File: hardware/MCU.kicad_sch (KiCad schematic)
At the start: 15 parts, among them SW1 MCP_HW_ADDR_SEL, SW2 MCP_N_RST, SW3 SW_SYS-PWR, U1 MCP23017_SO

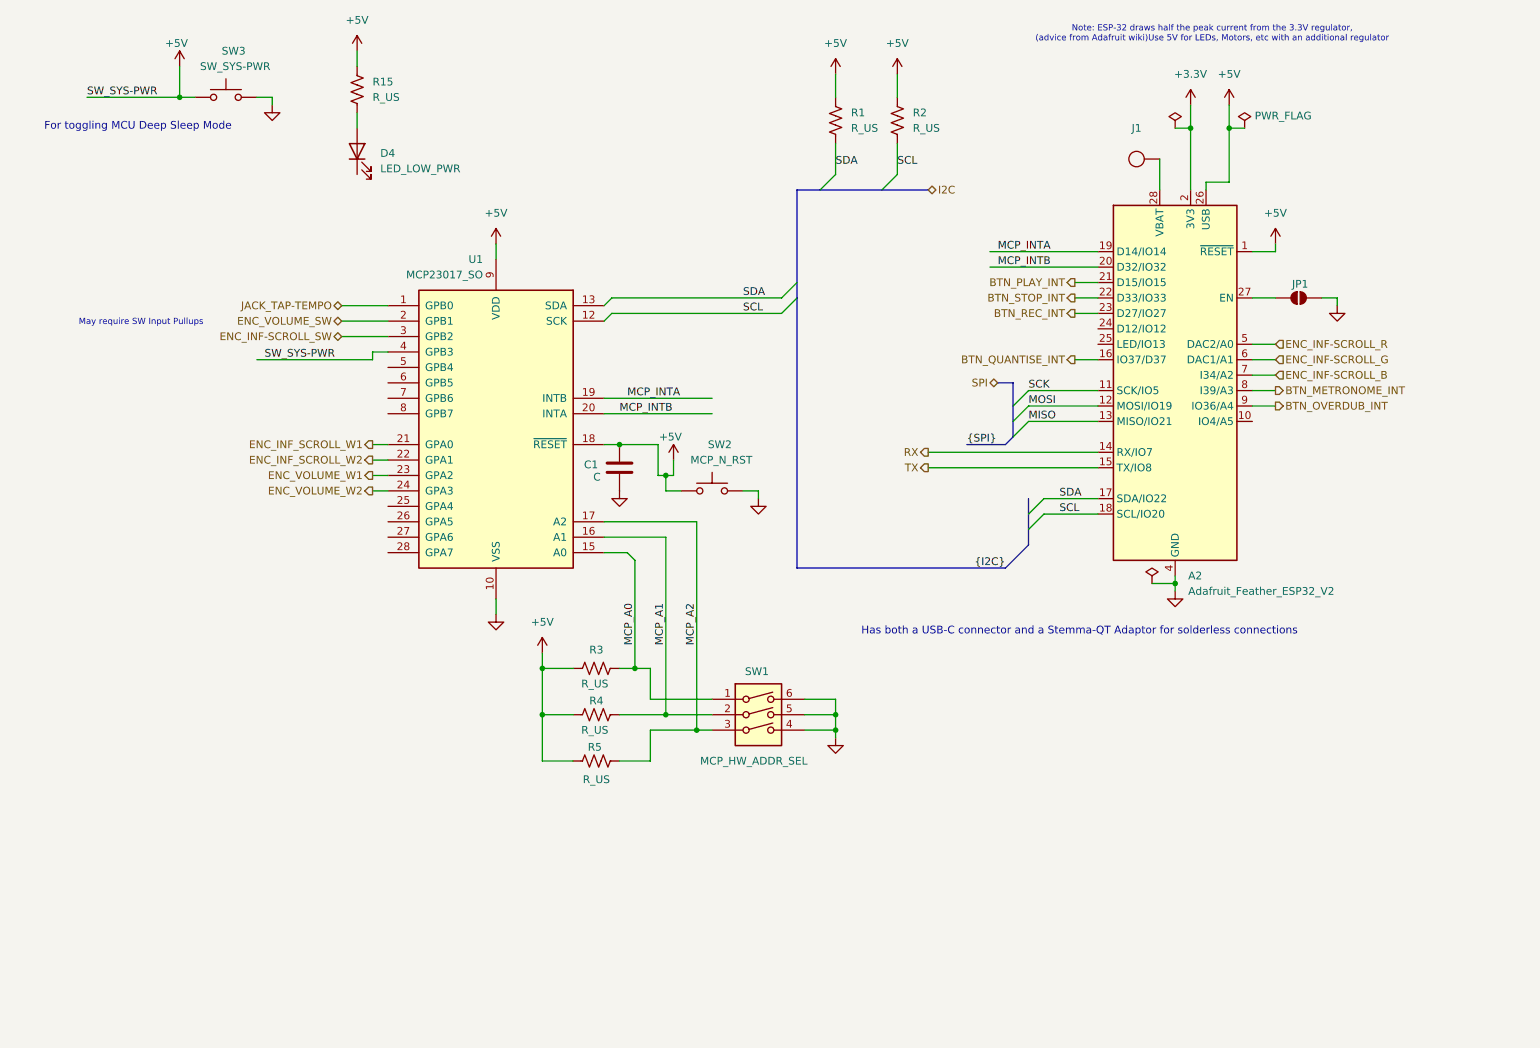
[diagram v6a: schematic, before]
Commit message: fix [HWE]: SYS_PWR_SW, BJT as a SX1509 Lvl Shifter
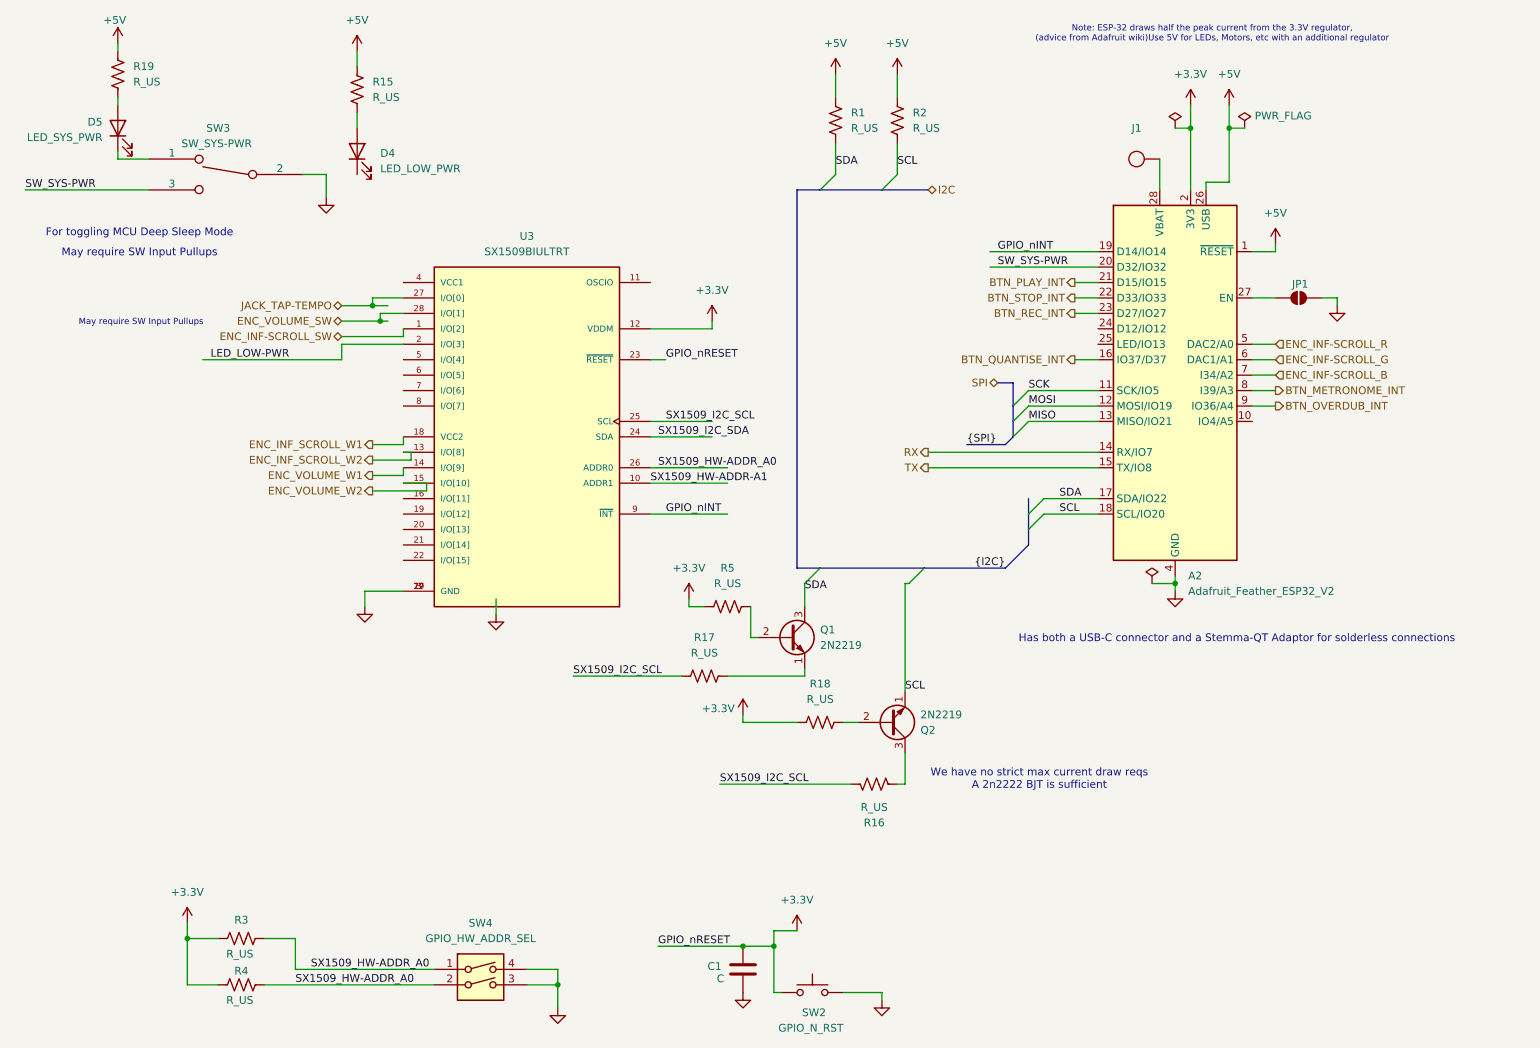
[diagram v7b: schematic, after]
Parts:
- removed SW1: MCP_HW_ADDR_SEL, 4ms_Switch:SW_DIP_SPSTx03_CTS_219-3MSTR, symbol 4ms_Switch:SW_DIP_x03_CTS_219-3MST
- removed U1: MCP23017_SO, Package_SO:SOIC-28W_7.5x17.9mm_P1.27mm, symbol Interface_Expansion:MCP23017_SO
- added D5: LED_SYS_PWR, symbol Device:LED
- added Q1, Q2: 2N2219, Package_TO_SOT_THT:TO-39-3, symbol Transistor_BJT:2N2219
- added R16, R17, R18, R19: R_US, symbol Device:R_US
- added SW4: GPIO_HW_ADDR_SEL, 4ms_Switch:SW_DIP_SPSTx02_CTS_219-2MSTR, symbol 4ms_Switch:SW_DIP_x02_CTS_219-2MST
- added U3: SX1509BIULTRT, SX1509BIULTRT:QFN40P400X400X60-29N, symbol SX1509:SX1509BIULTRT
- SW2: value MCP_N_RST -> GPIO_N_RST
- SW3: footprint (none) -> 4ms_Switch:Switch_Toggle_SPDT_SubMini; symbol Switch:SW_Push -> 4ms_Switch:Toggle_SPDT_SubMini_3pos; Manufacturer (none) -> Mountain Switch; Manufacturer 2 (none) -> (Posin's Supplier in China); Manufacturer 3 (none) -> (Posin Supplier in China Oct2020); Part Number (none) -> 108-2MS3T2B3M2QE-EVX; Part Number 2 (none) -> ST-0-103-C02-T000-RS; Part Number 3 (none) -> MS-100793-1172333; Production Stage (none) -> C; Specifications (none) -> SPDT, On/Off/On, SubMini toggle 3-position
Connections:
- net MCP_A1 is gone; now on net SX1509_HW-ADDR_A0: R4.2
- net +3.3V: now also C1.1, R3.1, R4.1, R5.1, SW2.1, R18.1, U3.12 (VDDM), U3.23 (~{RESET})
- net +5V: now also R19.1; no longer C1.1, R3.1, R4.1, R5.1, SW2.1, SW3.1
- net ENC_INF-SCROLL_SW: now also U3.1 (I/O[2])
- net ENC_INF_SCROLL_W1: now also U3.18 (VCC2)
- net ENC_INF_SCROLL_W2: now also U3.13 (I/O[8])
- net ENC_VOLUME_SW: now also U3.28 (I/O[1])
- net ENC_VOLUME_W1: now also U3.14 (I/O[9])
- net ENC_VOLUME_W2: now also U3.15 (I/O[10])
- net GND: now also SW4.3, SW4.4, U3.17 (GND), U3.29 (GND), U3.3 (GND)
- net JACK_TAP-TEMPO: now also U3.27 (I/O[0])
- net SCL: now also Q2.1 (E)
- net SDA: now also Q1.3 (C)
- net MCP_A0 renamed SX1509_HW-ADDR_A0
- net SX1509_HW-ADDR_A0: now also SW4.1, SW4.2, U3.26 (ADDR0)
- net MCP_A2: no longer names the net of R5.2
- net MCP_A2: now also Q1.2 (B)
- net MCP_INTA renamed GPIO_nINT
- net GPIO_nINT: now also U3.9 (~{INT})
- net MCP_INTB renamed SW_SYS-PWR
- net SW_SYS-PWR: now also SW3.3
- new net: Q1.1 (E), R17.2
- new net: Q2.2 (B), R18.2
- new net: Q2.3 (C), R16.2
- new net: D5.1 (K), SW3.1
- new net: D5.2 (A), R19.2
- new net LED_LOW-PWR: U3.2 (I/O[3])
- new net SX1509_HW-ADDR-A1: U3.10 (ADDR1)
- new net SX1509_I2C_SCL: R16.1, R17.1, U3.25 (SCL)
- new net SX1509_I2C_SDA: U3.24 (SDA)
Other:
- note added: "We have no strict max current draw reqs A 2n2222 BJT is sufficient"
- moved on the sheet: C1, R3, R4, SW2

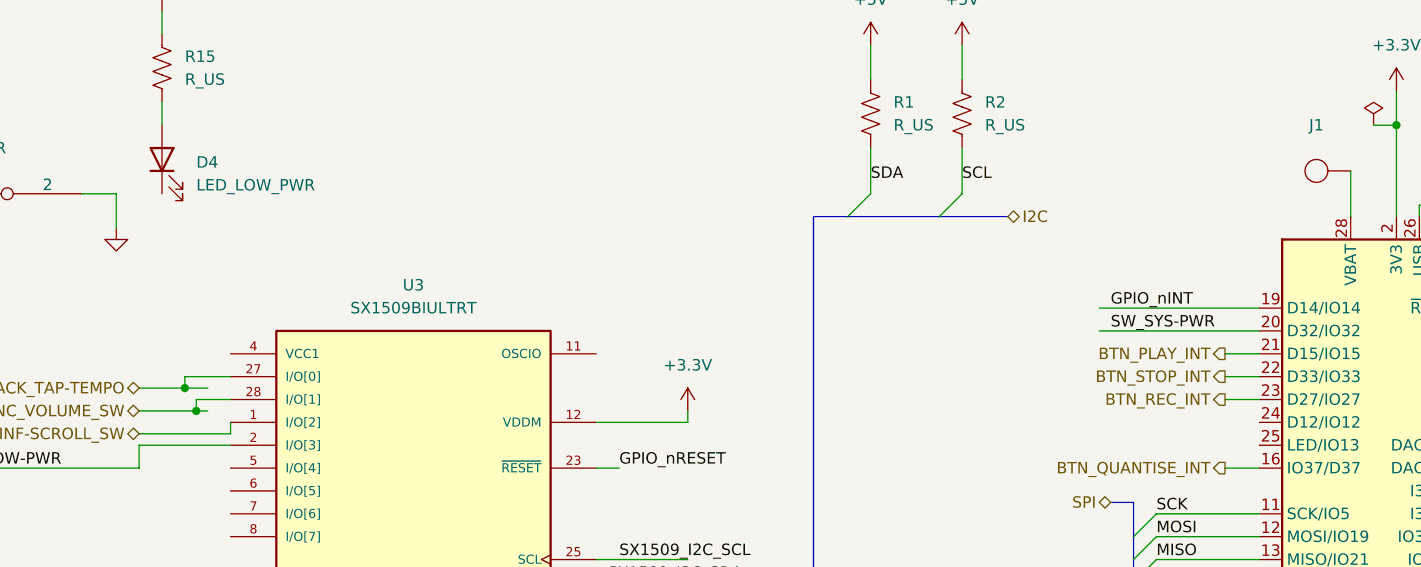
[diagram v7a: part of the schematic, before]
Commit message: feat [HWE]: Added LED_LOW_PWR & SW_SYS_PWR HW
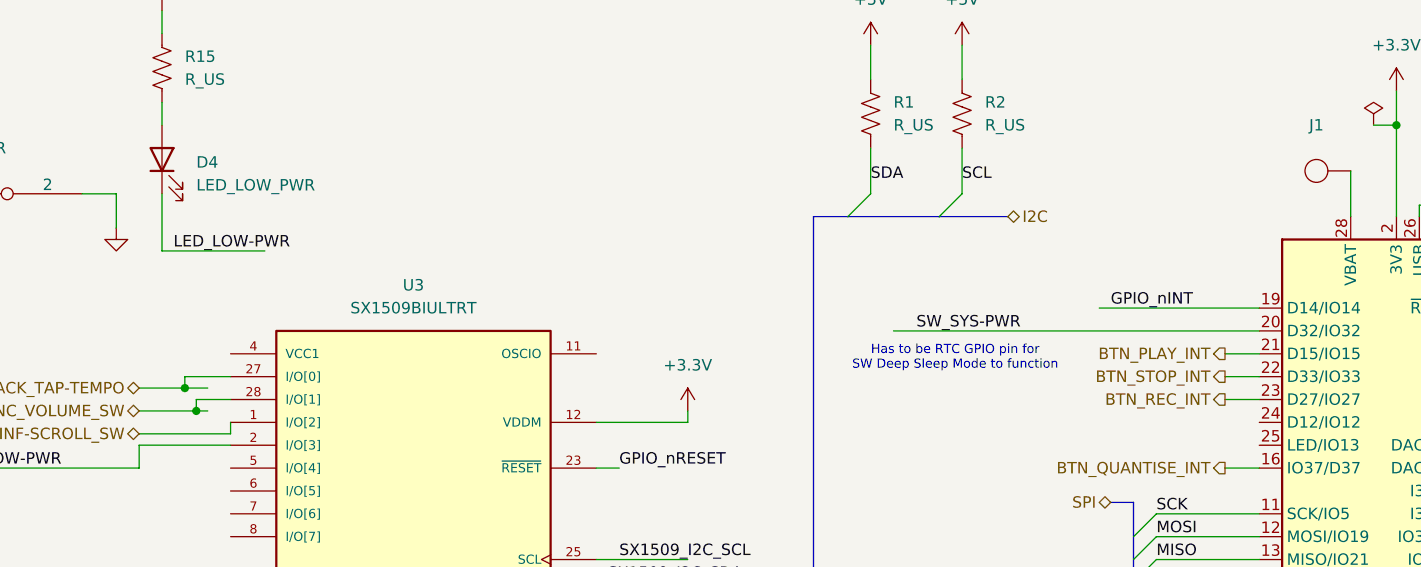
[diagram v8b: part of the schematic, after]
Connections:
- net LED_LOW-PWR: now also D4.1 (K)
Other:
- note added: "Has to be RTC GPIO pin for SW Deep Sleep Mode to function"
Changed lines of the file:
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@@
+		)
+	)
+	(text "Has to be RTC GPIO pin for \nSW Deep Sleep Mode to function"
+		(exclude_from_sim no)
+		(at 159.258 58.928 0)
+		(effects
+			(font
+				(size 1.016 1.016)
+			)
 		)
 	)
@@
 	(wire
 		(pts
-			(xy 175.26 55.88) (xy 193.04 55.88)
-		)
-		(stroke
-			(width 0)
-			(type default)
-		)
-	)
-	(wire
-		(pts
 			(xy 119.38 71.12) (xy 121.92 71.12)
 		)
@@
 	(wire
 		(pts
+			(xy 71.12 46.99) (xy 82.55 46.99)
+		)
+		(stroke
+			(width 0)
+			(type default)
+		)
+	)
+	(wire
+		(pts
 			(xy 73.66 62.23) (xy 76.2 62.23)
 		)
@@
 	(wire
 		(pts
+			(xy 71.12 40.64) (xy 71.12 46.99)
+		)
+		(stroke
+			(width 0)
+			(type default)
+		)
+	)
+	(wire
+		(pts
 			(xy 80.01 86.36) (xy 80.01 87.63)
 		)
@@
 		(pts
 			(xy 134.62 130.81) (xy 143.51 130.81)
+		)
+		(stroke
+			(width 0)
+			(type default)
+		)
+	)
+	(wire
+		(pts
+			(xy 152.4 55.88) (xy 193.04 55.88)
 		)
 		(stroke
@@
 		)
 	)
+	(label "LED_LOW-PWR"
+		(at 72.39 46.99 0)
+		(effects
+			(font
+				(size 1.27 1.27)
+			)
+			(justify left bottom)
+		)
+	)
 	(label "SX1509_HW-ADDR_A0"
 		(at 120.65 88.9 0)
@@
 	)
 	(label "SW_SYS-PWR"
-		(at 176.53 55.88 0)
-		(effects
-			(font
+		(at 154.94 55.88 0)
+		(effects
+			(font
